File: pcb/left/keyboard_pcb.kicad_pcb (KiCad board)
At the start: 2 copper layers, 138.8 x 89.9 mm, 32 parts, among them J1 TRRS, K00 KEYSW, K01 KEYSW, K02 KEYSW, K03 KEYSW, K04 KEYSW, K05 KEYSW, K10 KEYSW, K11 KEYSW, K12 KEYSW, K13 KEYSW, K14 KEYSW, K15 KEYSW, K20 KEYSW, K21 KEYSW, K22 KEYSW, K23 KEYSW, K24 KEYSW, K25 KEYSW, K30 KEYSW, K31 KEYSW, K32 KEYSW, U2 Pico

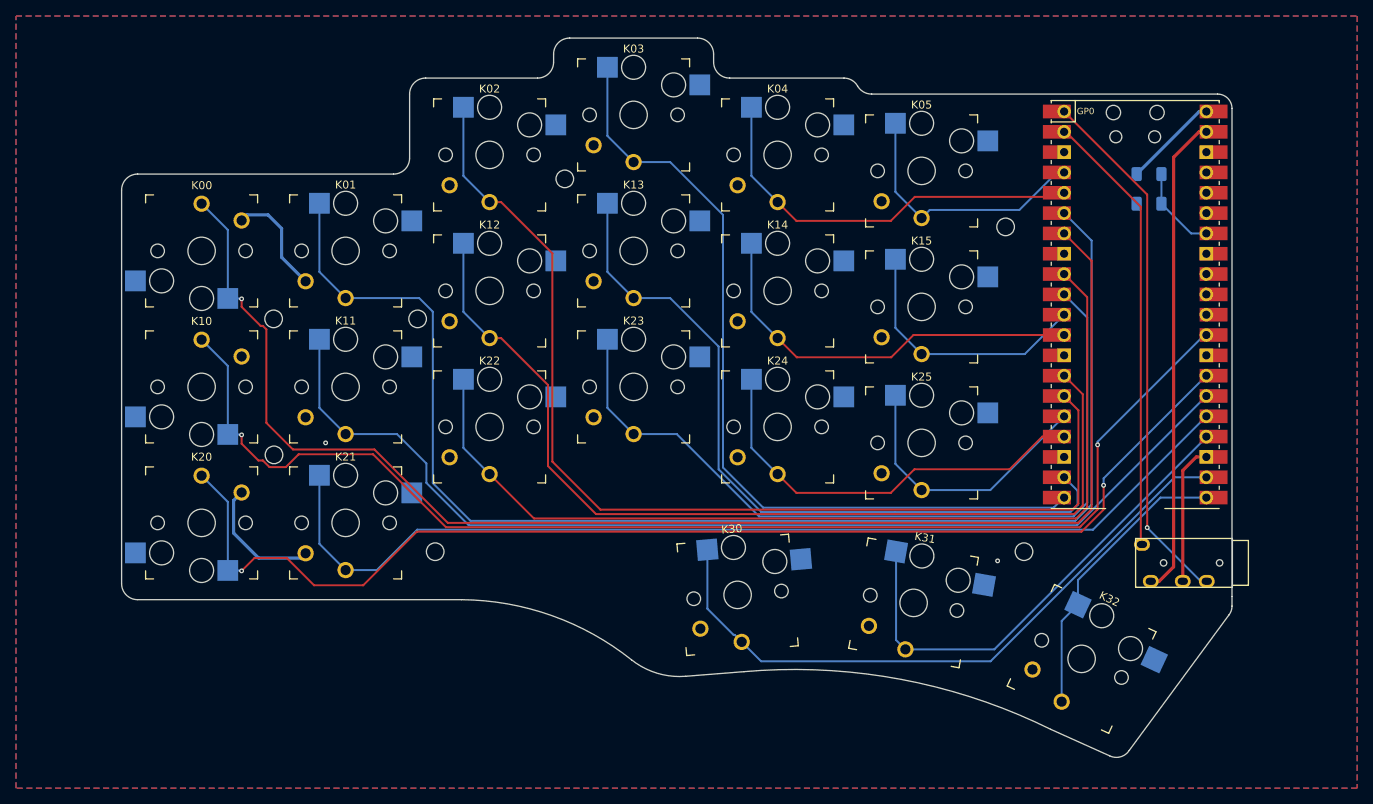
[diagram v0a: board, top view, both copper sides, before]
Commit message: feat: change choco switches to MX
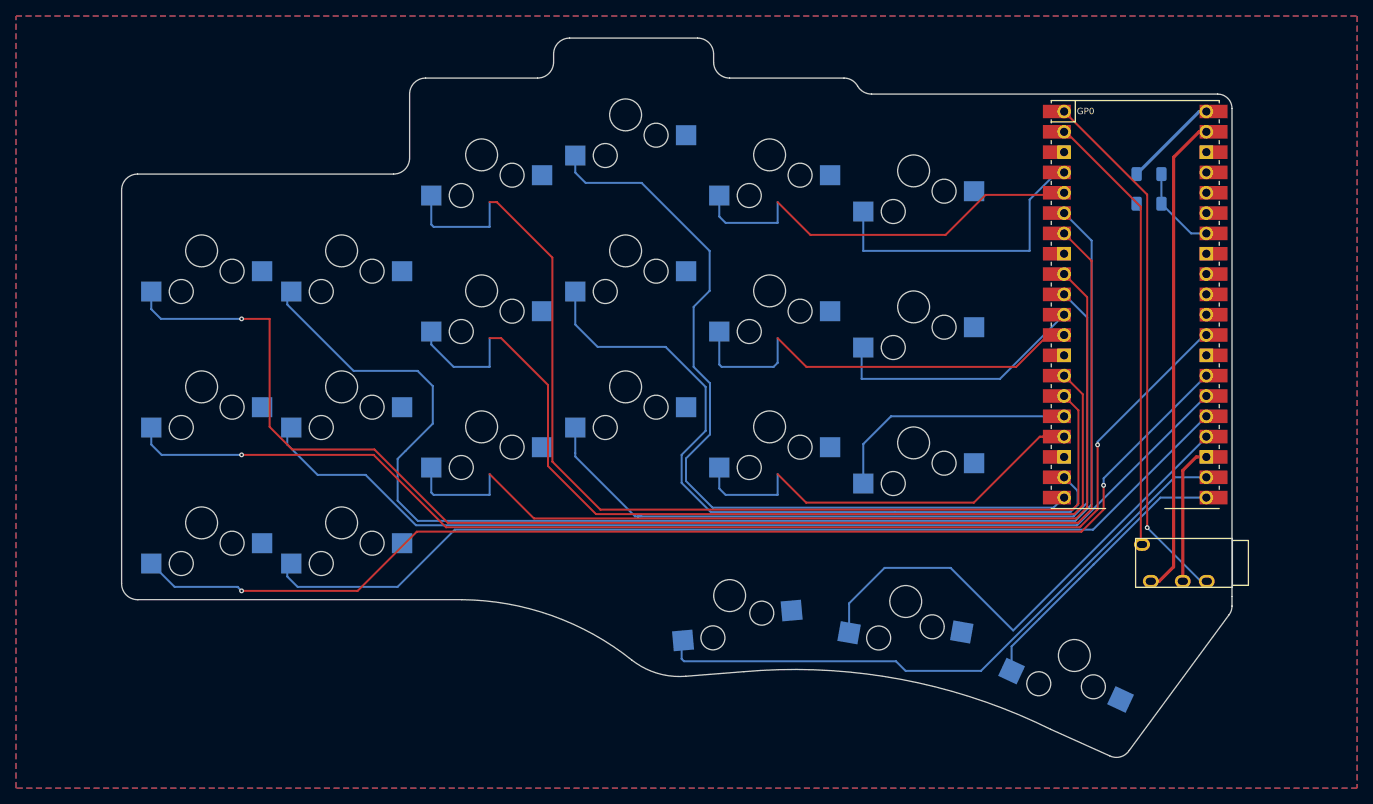
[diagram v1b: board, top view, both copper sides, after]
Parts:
- removed H1 (x2), H2, H3, H4 (x3): MountingHole, beekeeb_lib:MountingHole_2.2mm_M2-8mm
- K00, K01, K02, K03, K04, K05, K10, K11, K12, K13, K14, K15, K20, K21, K22, K23, K24, K25, K30, K31, K32: footprint keyswitches:Kailh_socket_PG1350_optional -> keyswitches:Kailh_socket_MX_3_pins_last
- moved K00 1.00 mm to (75.0, 70.0), turned to 0 degrees
- moved K10 1.00 mm to (75.0, 87.0), turned to 0 degrees
- moved K20 1.00 mm to (75.0, 104.0), turned to 0 degrees
- moved K01 0.50 mm to (92.5, 70.0)
- moved K11 0.50 mm to (92.5, 87.0)
- moved K21 0.50 mm to (92.5, 104.0)
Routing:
- net GND: track 47.4 -> 17.5 mm, vias 2 -> 0
- net /k11: track 133.6 -> 127.9 mm
- net /k05: track 33.4 -> 37.8 mm
- net /k20: track 150.8 -> 146.7 mm
- net /k10: track 157.3 -> 153.3 mm
- net /k24: track 52.9 -> 56.3 mm
- net /k30: track 82.0 -> 78.6 mm
- net /k25: track 34.8 -> 31.5 mm
- net /k23: track 102.1 -> 99.2 mm
- net /k21: track 128.8 -> 125.9 mm
- net /k14: track 51.2 -> 53.8 mm
- net /k01: track 169.2 -> 166.7 mm
- net /k31: track 61.4 -> 63.5 mm
- net /k04: track 51.4 -> 53.3 mm
- net /k00: track 176.8 -> 175.3 mm
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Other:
- board text added: "${REFERENCE}"

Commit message: fix: tracks & rotate 360 last 3 switches
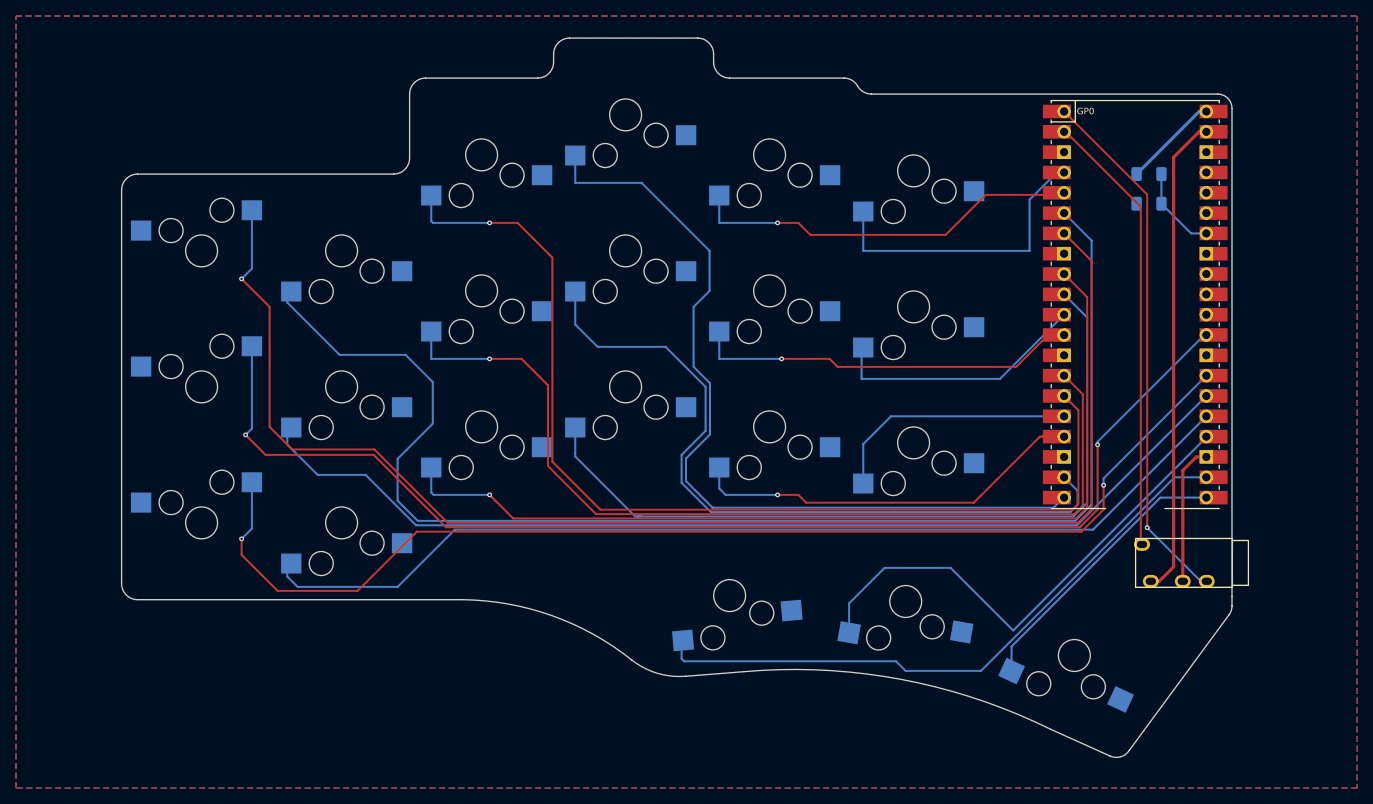
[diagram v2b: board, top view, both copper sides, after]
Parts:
- moved K00 2.00 mm to (73.0, 70.0), turned to 180 degrees
- moved K10 2.00 mm to (73.0, 87.0), turned to 180 degrees
- moved K20 2.00 mm to (73.0, 104.0), turned to 180 degrees
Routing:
- net /k14: track 53.8 -> 48.6 mm, vias 0 -> 1
- net /k02: track 133.1 -> 128.5 mm, vias 0 -> 1
- net /k12: track 120.5 -> 116.5 mm, vias 0 -> 1
- net /k24: track 56.3 -> 52.6 mm, vias 0 -> 1
- net /k22: track 121.1 -> 117.4 mm, vias 0 -> 1
- net /k04: track 53.3 -> 50.0 mm, vias 0 -> 1
- net /k10: track 153.3 -> 151.3 mm
- net /k00: track 175.3 -> 173.4 mm
- net /k20: track 146.7 -> 145.5 mm
- net /k03: track 103.8 -> 104.6 mm

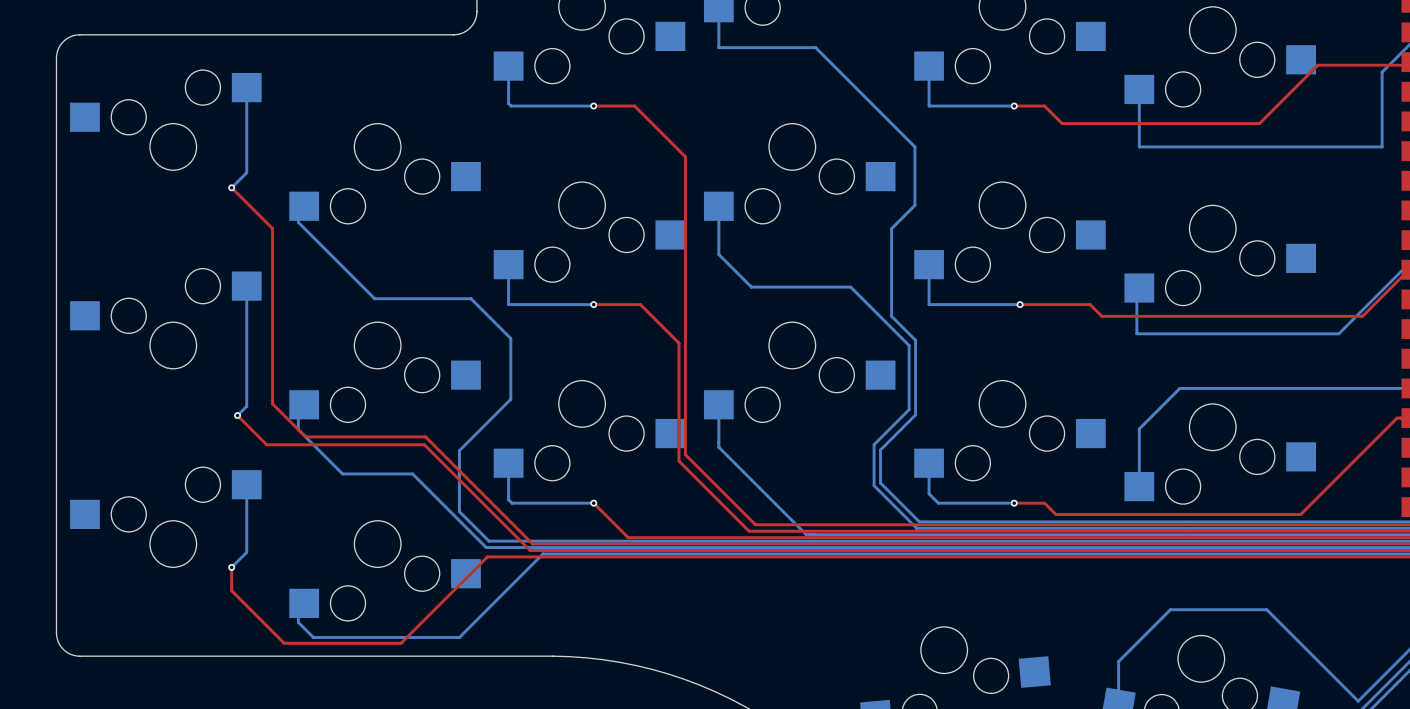
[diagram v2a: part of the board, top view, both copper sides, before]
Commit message: feat: centralize positive pins in back side board
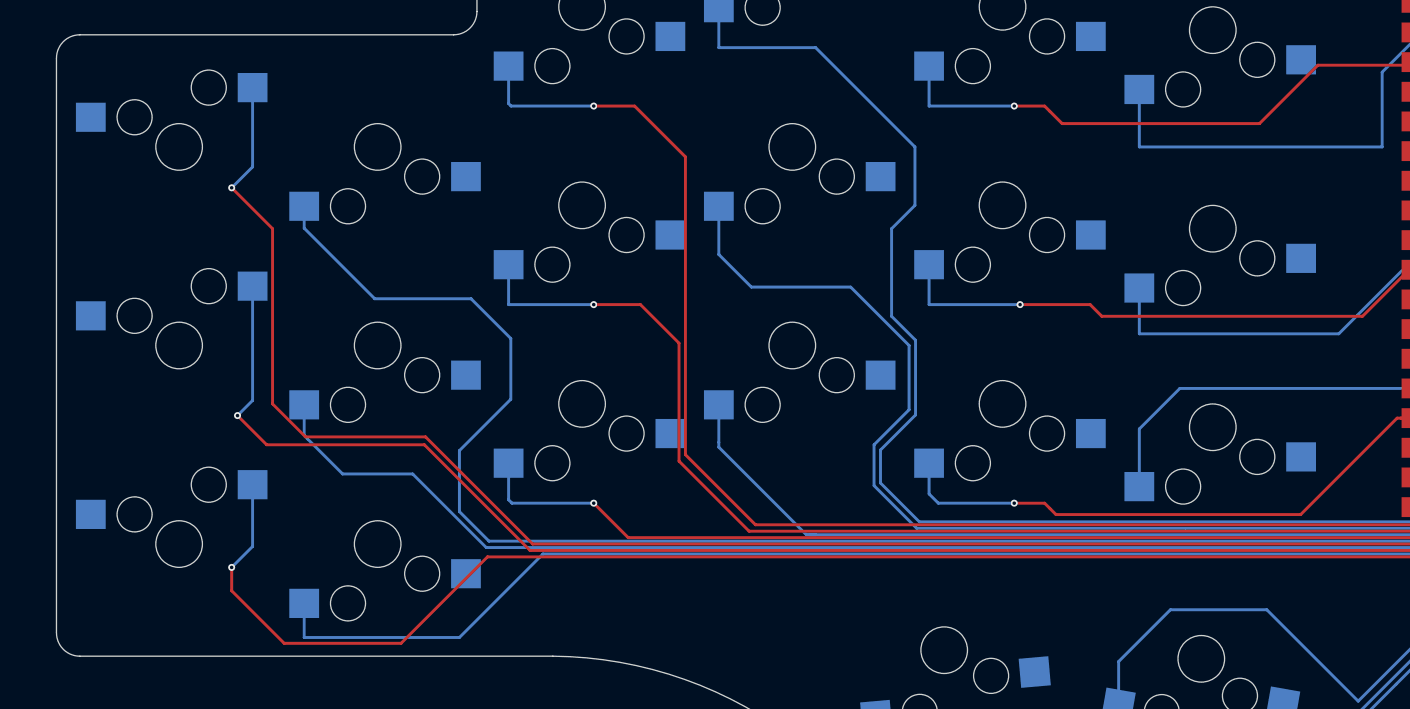
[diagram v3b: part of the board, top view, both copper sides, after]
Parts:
- moved K00 0.50 mm to (73.5, 70.0)
- moved K10 0.50 mm to (73.5, 87.0)
- moved K20 0.50 mm to (73.5, 104.0)
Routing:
- net /k21: track 125.9 -> 127.3 mm
- net /k20: track 145.5 -> 146.7 mm
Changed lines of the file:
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@@
 	(footprint "keyswitches:Kailh_socket_MX_3_pins_last"
 		(layer "F.Cu")
-		(at 73 87 180)
+		(at 73.5 87 180)
 		(descr "MX-style keyswitch with Kailh socket mount")
 		(tags "MX,cherry,gateron,kailh,pg1511,socket")
@@
 	(footprint "keyswitches:Kailh_socket_MX_3_pins_last"
 		(layer "F.Cu")
-		(at 73 104 180)
+		(at 73.5 104 180)
 		(descr "MX-style keyswitch with Kailh socket mount")
 		(tags "MX,cherry,gateron,kailh,pg1511,socket")
@@
 	(footprint "keyswitches:Kailh_socket_MX_3_pins_last"
 		(layer "F.Cu")
-		(at 73 70 180)
+		(at 73.5 70 180)
 		(descr "MX-style keyswitch with Kailh socket mount")
 		(tags "MX,cherry,gateron,kailh,pg1511,socket")
@@
 	)
 	(segment
-		(start 80.29 72.21)
-		(end 80.29 64.92)
+		(start 80.79 64.92)
+		(end 80.79 71.71)
 		(width 0.25)
 		(layer "B.Cu")
@@
 	)
 	(segment
-		(start 79 73.5)
-		(end 80.29 72.21)
+		(start 80.79 71.71)
+		(end 79 73.5)
 		(width 0.25)
 		(layer "B.Cu")
@@
 	)
 	(segment
-		(start 91.25 83)
-		(end 99.5 83)
+		(start 185.25 101.704062)
+		(end 185.25 68.7148)
 		(width 0.25)
 		(layer "B.Cu")
@@
 	)
 	(segment
-		(start 98.5 101.222182)
-		(end 101.027337 103.749519)
+		(start 185.25 68.7148)
+		(end 181.8132 65.278)
 		(width 0.25)
 		(layer "B.Cu")
@@
 	)
 	(segment
-		(start 102.9 91.6)
-		(end 98.5 96)
+		(start 84.71 75.08)
+		(end 85.21 75.08)
 		(width 0.25)
 		(layer "B.Cu")
@@
 	)
 	(segment
-		(start 84.71 76.46)
-		(end 91.25 83)
+		(start 98.5 101.222182)
+		(end 101.027337 103.749519)
 		(width 0.25)
 		(layer "B.Cu")
@@
 	)
 	(segment
-		(start 99.5 83)
-		(end 102.9 86.4)
+		(start 91.25 83)
+		(end 99.5 83)
 		(width 0.25)
 		(layer "B.Cu")
@@
 	)
 	(segment
-		(start 185.25 68.7148)
-		(end 181.8132 65.278)
+		(start 85.21 75.08)
+		(end 85.21 76.96)
 		(width 0.25)
 		(layer "B.Cu")
@@
 	)
 	(segment
-		(start 102.9 86.4)
-		(end 102.9 91.6)
+		(start 102.9 91.6)
+		(end 98.5 96)
 		(width 0.25)
 		(layer "B.Cu")
@@
 	)
 	(segment
-		(start 84.71 75.08)
-		(end 84.71 76.46)
+		(start 101.027337 103.749519)
+		(end 183.204543 103.749519)
 		(width 0.25)
 		(layer "B.Cu")
@@
 	)
 	(segment
-		(start 101.027337 103.749519)
-		(end 183.204543 103.749519)
+		(start 99.5 83)
+		(end 102.9 86.4)
 		(width 0.25)
 		(layer "B.Cu")
@@
 	)
 	(segment
-		(start 185.25 101.704062)
-		(end 185.25 68.7148)
+		(start 85.21 76.96)
+		(end 91.25 83)
+		(width 0.25)
+		(layer "B.Cu")
+		(net 3)
+	)
+	(segment
+		(start 102.9 86.4)
+		(end 102.9 91.6)
 		(width 0.25)
 		(layer "B.Cu")
@@
 	)
 	(segment
+		(start 80.79 91.71)
+		(end 79.5 93)
+		(width 0.25)
+		(layer "B.Cu")
+		(net 8)
+	)
+	(segment
 		(start 186 94.25)
 		(end 186 93.860769)
@@
 	)
 	(segment
-		(start 80.29 92.21)
-		(end 80.29 81.92)
+		(start 80.79 81.92)
+		(end 80.79 91.71)
 		(width 0.25)
 		(layer "B.Cu")
@@
 	)
 	(segment
-		(start 79.5 93)
-		(end 80.29 92.21)
+		(start 85.21 94.71)
+		(end 85.5 95)
 		(width 0.25)
 		(layer "B.Cu")
-		(net 8)
+		(net 9)
 	)
 	(segment
-		(start 84.71 94.21)
-		(end 88.5 98)
+		(start 85.21 92.08)
+		(end 85.21 94.71)
 		(width 0.25)
 		(layer "B.Cu")
@@
 	)
 	(segment
-		(start 84.71 92.08)
-		(end 84.71 94.21)
+		(start 85.5 95)
+		(end 88.5 98)
 		(width 0.25)
 		(layer "B.Cu")
@@
 	)
 	(segment
-		(start 173.7912 86)
-		(end 181.8132 77.978)
+		(start 156.71 86)
+		(end 173.7912 86)
 		(width 0.25)
 		(layer "B.Cu")
@@
 	)
 	(segment
-		(start 156.5 82.29)
-		(end 156.5 86)
+		(start 173.7912 86)
+		(end 181.8132 77.978)
 		(width 0.25)
 		(layer "B.Cu")
@@
 	)
 	(segment
-		(start 156.5 86)
-		(end 173.7912 86)
+		(start 156.71 82.08)
+		(end 156.71 86)
 		(width 0.25)
 		(layer "B.Cu")
@@
 	)
 	(segment
-		(start 79 106)
-		(end 80.29 104.71)
+		(start 80.79 98.92)
+		(end 80.79 104.21)
+		(width 0.25)
+		(layer "B.Cu")
+		(net 14)
+	)
+	(segment
+		(start 80.79 104.21)
+		(end 79 106)
 		(width 0.25)
 		(layer "B.Cu")
@@
 	)
 	(segment
-		(start 186.75 99.3)
-		(end 186.75 98.4412)
+		(start 81 99.63)
+		(end 80.29 98.92)
 		(width 0.25)
 		(layer "B.Cu")
@@
 	)
 	(segment
-		(start 80.29 104.71)
-		(end 80.29 98.92)
+		(start 186.75 99.3)
+		(end 186.75 98.4412)
 		(width 0.25)
 		(layer "B.Cu")
@@
 	)
 	(segment
-		(start 84.71 109.08)
-		(end 84.71 110.71)
+		(start 85.21 109.08)
+		(end 85.21 112)
 		(width 0.25)
 		(layer "B.Cu")
@@
 	)
 	(segment
-		(start 185.42264 104.84856)
-		(end 199.5932 90.678)
+		(start 84.71 109.08)
+		(end 84.71 110.21)
 		(width 0.25)
 		(layer "B.Cu")
@@
 	)
 	(segment
-		(start 86 112)
-		(end 98.5 112)
+		(start 185.42264 104.84856)
+		(end 199.5932 90.678)
 		(width 0.25)
 		(layer "B.Cu")
@@
 	)
 	(segment
-		(start 84.71 110.71)
-		(end 86 112)
+		(start 85.21 112)
+		(end 98.5 112)
 		(width 0.25)
 		(layer "B.Cu")
